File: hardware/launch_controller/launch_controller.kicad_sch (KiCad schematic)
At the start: 32 parts, among them IC1 ADIN1110BCPZ, J1 Screw_Terminal_01x03, T1 Transformer_1P_1S, Y1 25MHz

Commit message: feat(scm): STM32 added.
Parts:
- added C17, C9: 1μF, Package_TO_SOT_SMD:TSOT-23-6, symbol Device:C_Small
- added C18, C19: 22μF, symbol Device:C_Small
- added D2: LED, Package_DFN_QFN:Texas_RPU0010A_VQFN-HR-10_2x2mm_P0.5mm, symbol Device:LED
- added J2: Conn_01x02_Socket, Converter_DCDC:Converter_DCDC_Murata_MYRxP, symbol Connector:Conn_01x02_Socket
- added L1: 4.7μH, Package_SO:SOIC-16_3.9x9.9mm_P1.27mm, symbol Device:L_Small
- added R7: 1kΩ, symbol Device:R
- added R8: 4.7kΩ, symbol Device:R
- added U1: STM32U575VITx, Package_QFP:LQFP-100_14x14mm_P0.5mm, symbol MCU_ST_STM32U5:STM32U575VITx
- added U2: AP63205WU, Package_TO_SOT_SMD:TSOT-23-6, symbol Regulator_Switching:AP63205WU
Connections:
- net +3.3V: now also R4.1, C18.1, C19.2, L1.2, R7.1, R8.1, U1.100 (VDD), U1.11 (VDD), U1.21 (VREF+), U1.22 (VDDA), U1.28 (VDD), U1.50 (VDD), U1.75 (VDD), U2.1 (FB)
- net EC_INT: now also U1.67 (PA8)
- net EC_RESET: now also U1.23 (PA0)
- net EC_SPI_CS: now also U1.29 (PA4)
- net EC_SPI_MISO: now also U1.31 (PA6)
- net EC_SPI_MOSI: now also U1.32 (PA7)
- net EC_SPI_SCLK: now also U1.30 (PA5)
- net GND: now also C18.2, C19.1, C9.2, J2.2 (Pin_2), U1.10 (VSS), U1.19 (VSSA), U1.27 (VSS), U1.49 (VSS), U1.74 (VSS), U1.99 (VSS), U2.4 (GND); no longer R4.1
- net EC_STATUS: now reaches IC1.3 (LED_0)
- net EC_STATUS: now also D2.1 (K), R8.2
- new net: C9.1, J2.1 (Pin_1), U2.2 (EN), U2.3 (IN)
- new net: C17.1, L1.1, U2.5 (SW)
- new net: C17.2, U2.6 (BST)
- new net: D2.2 (A), R7.2
- new net UART_STM32_RX: U1.69 (PA10)
- new net UART_STM32_TX: U1.68 (PA9)
- no-connect marks 15 -> 14
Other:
- note added: "Conntroller"
- note removed: "Controller"

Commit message: feat(scm): USB added.
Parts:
- removed U2: AP63205WU, Package_TO_SOT_SMD:TSOT-23-6, symbol Regulator_Switching:AP63205WU
- added C20: 0.1μF, symbol Device:C_Small
- added D3: LED, Package_DFN_QFN:Texas_RPU0010A_VQFN-HR-10_2x2mm_P0.5mm, symbol Device:LED
- added J3: USB_B, symbol Connector:USB_B
- added R10, R9: R, symbol Device:R
- added R11: 4.7μF, symbol Device:R
- added R18: 1kΩ, symbol Device:R
- added R19: 10kΩ, symbol Device:R
- added R20: 22kΩ, symbol Device:R
- added U2: AP63203WU, Package_TO_SOT_SMD:TSOT-23-6, symbol Regulator_Switching:AP63203WU
- added U3: SN74LVC257AD, D16, symbol pCloud:SN74LVC257AD
- added U4: FT232H, symbol Interface_USB:FT232H
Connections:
- net +3.3V: now also U1.6 (VBAT), U1.73 (VDDUSB), R18.1, U2.1 (FB), U3.16 (VCC)
- net EC_SPI_CS: now also U3.4 (1Y); no longer U1.29 (PA4)
- net EC_SPI_MISO: now also U3.9 (3Y); no longer U1.31 (PA6)
- net EC_SPI_MOSI: now also U3.12 (4Y); no longer U1.32 (PA7)
- net EC_SPI_SCLK: now also U3.7 (2Y); no longer U1.30 (PA5)
- net GND: now also U1.20 (VREF-), C20.1, D3.1 (K), R10.2, R11.1, R20.1, U2.4 (GND), U3.15 (*OE), U3.8 (GND)
- net at C9.1, J2.1 (Pin_1): now also R9.1, U2.2 (EN), U2.3 (IN)
- net at C17.1, L1.1: now also U2.5 (SW)
- net at C17.2: now also U2.6 (BST)
- net at U1.14 (NRST): now also C20.2
- net ADC: now reaches U1.24 (PA1)
- net ADC: now also R10.1, R9.2
- net at U1.48 (VCAP): now also R11.2
- new net: R19.2, R20.2, U3.1 (*A/B)
- new net: D3.2 (A), R18.2
- new net MCU_SPI_CS: U1.29 (PA4), U3.2 (1A)
- new net MCU_SPI_MISO: U1.31 (PA6), U3.11 (3A)
- new net MCU_SPI_MOSI: U1.32 (PA7), U3.14 (4A)
- new net MCU_SPI_SCLK: U1.30 (PA5), U3.5 (2A)
- new net VBUS: J3.1 (VBUS), R19.1
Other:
- note added: "MCU"
- note added: "Power"
- moved on the sheet: C17, C18, C19, C9, D2, J2, L1, R7, R8, U1

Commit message: feat(scm): Draft v1.
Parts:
- removed U3: SN74LVC257AD, D16, symbol pCloud:SN74LVC257AD
- removed U4: FT232H, symbol Interface_USB:FT232H
- added C21, C22, C27: 0.1μF, symbol Device:C_Small
- added C23: 4.7μF, symbol Device:C_Small
- added C24: 10nF, symbol Device:C_Small
- added C25, C26: 47pF, symbol Device:C_Small
- added D4, D5: D_Small, symbol Device:D_Small
- added D6, D7, D8, D9: LED, symbol Device:LED
- added FB1: FerriteBead, symbol Device:FerriteBead
- added R21, R22, R23, R24, R25, R26, R27, R28: 10kΩ, symbol Device:R
- added SW1, SW2, SW3, SW4, SW5: SW_SPST, symbol Switch:SW_SPST
- added U3: FT230XS, Package_SO:SSOP-16_3.9x4.9mm_P0.635mm, symbol Interface_USB:FT230XS
- C9: value 1μF -> 10μF
- R19: value 10kΩ -> 27Ω
- R20: value 22kΩ -> 27Ω
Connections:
- net MCU_SPI_CS is gone; now on net EC_SPI_CS: U1.29 (PA4)
- net MCU_SPI_MISO is gone; now on net EC_SPI_MISO: U1.31 (PA6)
- net MCU_SPI_MOSI is gone; now on net EC_SPI_MOSI: U1.32 (PA7)
- net MCU_SPI_SCLK is gone; now on net EC_SPI_SCLK: U1.30 (PA5)
- net +3.3V: now also R21.1, R22.1, R23.1, R24.1, R25.1, R26.1, R27.1, R28.1
- net ADC: now also C27.2
- net GND: now also J3.4 (GND), J3.SH (Shield), C21.1, C22.1, C23.1, C24.1, C25.2, C26.1, C27.1, D6.1 (K), D6.2 (A), D7.1 (K), D7.2 (A), D8.1 (K), D8.2 (A), D9.1 (K), D9.2 (A), R22.2, R24.2, R26.2, R28.2, SW1.2 (B), SW2.2 (B), SW3.2 (B), SW4.2 (B), U3.13 (GND), U3.5 (GND); no longer R20.1
- net UART_STM32_RX: now also U3.1 (TXD)
- net UART_STM32_TX: now also U3.4 (RXD)
- net VBUS: now also C24.2, D5.2 (A), FB1.1; no longer R19.1
- net at C9.1, R9.1, U2.2 (EN)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: now also D4.1 (K), D5.1 (K); no longer J2.1 (Pin_1)
- net at R20.2: now also U3.9 (USBDM); no longer R19.2
- net at J3.2 (D-): now also R20.1, C26.2
- net at J3.3 (D+): now also R19.1, C25.1
- new net: D4.2 (A), SW5.2 (B)
- new net: C22.2, C23.2, FB1.2, U3.12 (VCC)
- new net: C21.2, U3.10 (3V3OUT), U3.11 (~{RESET}), U3.3 (VCCIO)
- new net: R19.2, U3.8 (USBDP)
- new net +12V: J2.1 (Pin_1), SW5.1 (A)
- new net GPIO_DUMP: R23.2, SW2.1 (A)
- new net GPIO_FILL: R21.2, R27.2, SW1.1 (A), SW4.1 (A)
- new net GPIO_GOX: R25.2, SW3.1 (A)
- no-connect marks 14 -> 93
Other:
- note added: "Hybrid Circit"
- note added: "Status"
- note added: "Switches"
- note added: "USB"
- note removed: "Connector"
- moved on the sheet: C17, C18, C19, C20, C9, D2, D3, J2, L1, R10, R11, R18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

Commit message: fix(scm): Hybrid circit updated.
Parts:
- added C28, C29: 47pF, symbol Device:C_Small
- added D10: D_TVS_Dual_AAC, Package_TO_SOT_SMD:TSOT-23-5_HandSoldering, symbol Device:D_TVS_Dual_AAC
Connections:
- net EC_RXN: now also R13.1, R15.1; no longer R12.2, R16.1
- net EC_RXP: now also R12.2, R17.1; no longer R12.1, R15.1
- net EC_TXN: now also R12.1, R14.1; no longer R13.2, R17.1
- net EC_TXP: now also R13.2, R16.1; no longer R13.1, R14.1
- net GND: now also C28.2, C29.2, D10.3 (common)
- net at C15.1, R16.2, R17.2: now also D1.2 (A2)
- net at C14.1, R14.2, R15.2: now also D1.1 (A1)
- net at J1.1 (Pin_1), T1.4 (SB): now also C28.1, D10.2 (A2)
- net SPE_1: no longer names the net of C14.2, T1.1 (AA)
- net SPE_1: no longer D1.1 (A1)
- net SPE_2: no longer names the net of C15.2, T1.2 (AB)
- net SPE_2: no longer D1.2 (A2)
- new net: C29.1, D10.1 (A1)
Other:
- moved on the sheet: C14, C15, C16, D1, J1, R12, R13, R14, R15, T1

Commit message: feat(scm): USB Surge Protection Circuit
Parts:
- added C30, C31, C32, C33, C34, C35, C36, C37: 0.1nF, symbol Device:C_Small
- added C38: 1μF, symbol Device:C_Small
- added C39: 10μF, symbol Device:C_Small
- added C40: 4.7nF, symbol Device:C_Small
- added R11: 1MΩ, symbol Device:R
- added SW6: SW_SPST, symbol Switch:SW_SPST
- added U5: USBLC6-2P6, Package_TO_SOT_SMD:SOT-666, symbol Power_Protection:USBLC6-2P6
- C1: value 0.01μF -> 0.1μF
- C11: renamed from R11; symbol Device:R -> Device:C_Small
- C17: value 1μF -> 0.1μF
- L1: value 4.7μH -> 3.9μH
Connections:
- net +3.3V: now also C1.2, C10.2, C11.2, C12.1, C13.1, C16.2, C18.2, C19.1, C2.2, C20.1, C21.1, C22.1, C23.1, C24.1, C25.2, C26.1, C27.1, C28.2, C29.2, C3.1, C4.1, C5.1, C6.1, C7.2, C8.2, C9.2, D1.3 (common), D10.3 (common), D3.1 (K), D6.1 (K), D6.2 (A), D7.1 (K), D7.2 (A), D8.1 (K), D8.2 (A), D9.1 (K), D9.2 (A), IC1.41 (GND), J2.2 (Pin_2), J3.4 (GND), R10.2, R22.2, R24.2, R26.2, R28.2, R3.1, R5.2, SW1.2 (B), SW2.2 (B), SW3.2 (B), SW4.2 (B), U1.10 (VSS), U1.19 (VSSA), U1.20 (VREF-), U1.27 (VSS), U1.49 (VSS), U1.74 (VSS), U1.99 (VSS), U2.4 (GND), U3.13 (GND), U3.5 (GND), C30.1, C31.1, C32.1, C33.1, C34.1, C35.1, C36.1, C37.1, C38.1, C39.1, C40.1, R11.2, U5.2 (GND)
- net VBUS: now also U5.5 (VBUS)
- net at D1.2 (A2), R16.2, R17.2: now also T1.2 (AB); no longer C15.1
- net at C25.1, R19.1: now also U5.6 (I/O1); no longer J3.3 (D+)
- net at D1.1 (A1), R14.2, R15.2: now also T1.1 (AA); no longer C14.1
- net at C14.2: now also C28.1, D10.2 (A2), J1.1 (Pin_1); no longer T1.1 (AA)
- net at C11.2: no longer U1.48 (VCAP)
- net at C26.2, R20.1: now also U5.4 (I/O2); no longer J3.2 (D-)
- net at C15.2: now also J1.2 (Pin_2); no longer T1.2 (AB)
- net at T1.3 (SA): now also C15.1; no longer J1.2 (Pin_2)
- net at C20.2: now also SW6.1 (A); no longer U1.14 (NRST)
- removed net GND: C1.2, C10.2, C11.1, C11.2, C12.1, C13.1, C16.2, C18.2, C19.1, C2.2, C20.1, C21.1, C22.1, C23.1, C24.1, C25.2, C26.1, C27.1, C28.2, C29.2, C3.1, C4.1, C5.1, C6.1, C7.2, C8.2, C9.2, D1.3 (common), D10.3 (common), D3.1 (K), D6.1 (K), D6.2 (A), D7.1 (K), D7.2 (A), D8.1 (K), D8.2 (A), D9.1 (K), D9.2 (A), IC1.41 (GND), J2.2 (Pin_2), J3.4 (GND), J3.SH (Shield), R10.2, R22.2, R24.2, R26.2, R28.2, R3.1, R5.2, SW1.2 (B), SW2.2 (B), SW3.2 (B), SW4.2 (B), U1.10 (VSS), U1.19 (VSSA), U1.20 (VREF-), U1.27 (VSS), U1.49 (VSS), U1.74 (VSS), U1.99 (VSS), U2.4 (GND), U3.13 (GND), U3.5 (GND)
- new net: C30.2, C31.2, C32.2, C33.2, C34.2, C35.2, C36.2, C37.2, C38.2, C39.2
- new net: C14.1, T1.4 (SB)
- new net: J3.2 (D-), U5.3 (I/O2)
- new net: J3.3 (D+), U5.1 (I/O1)
- new net: SW6.2 (B), U1.14 (NRST)
- new net Earth: C40.2, J3.SH (Shield), R11.1
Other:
- moved on the sheet: C20, C25, C26, FB1, R19, R20, T1

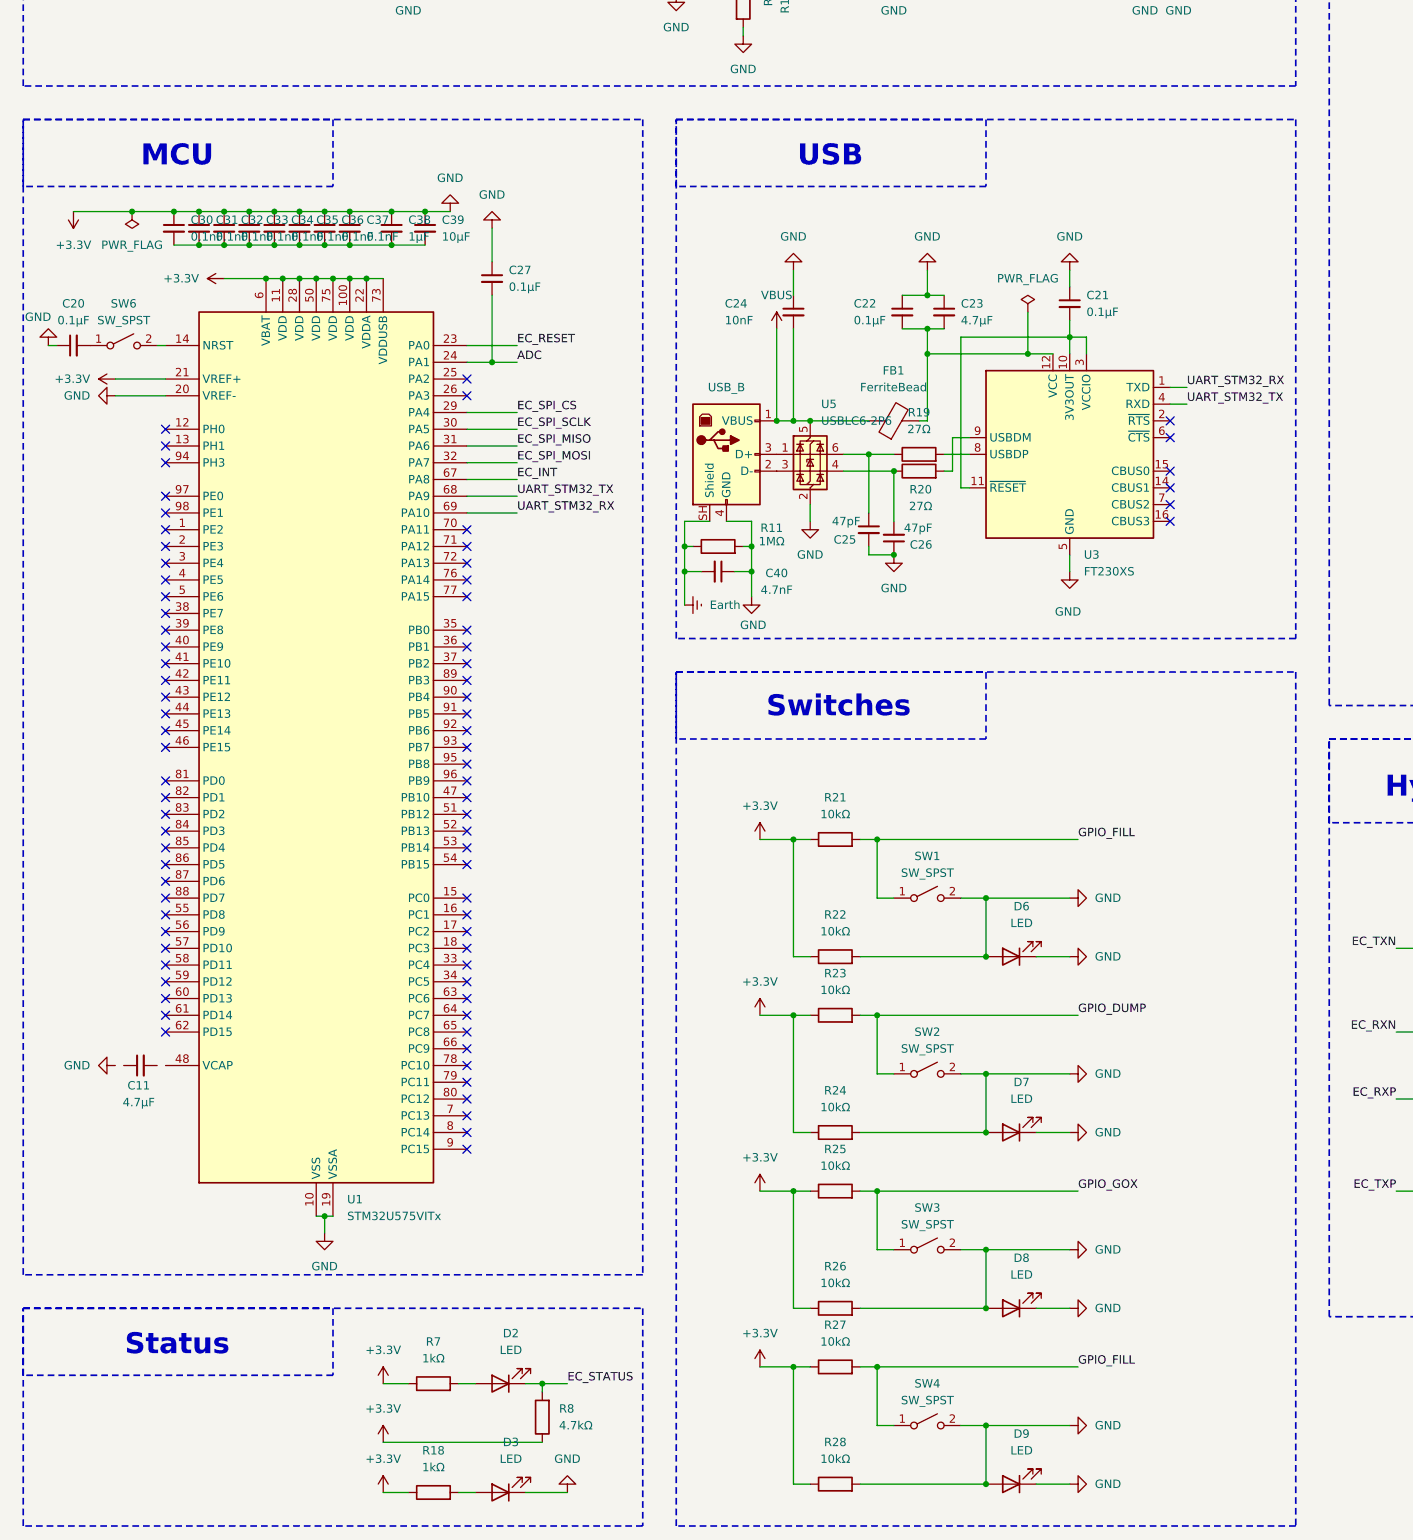
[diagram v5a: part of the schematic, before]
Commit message: fix(scm): TBD62083A amd SWD are added.
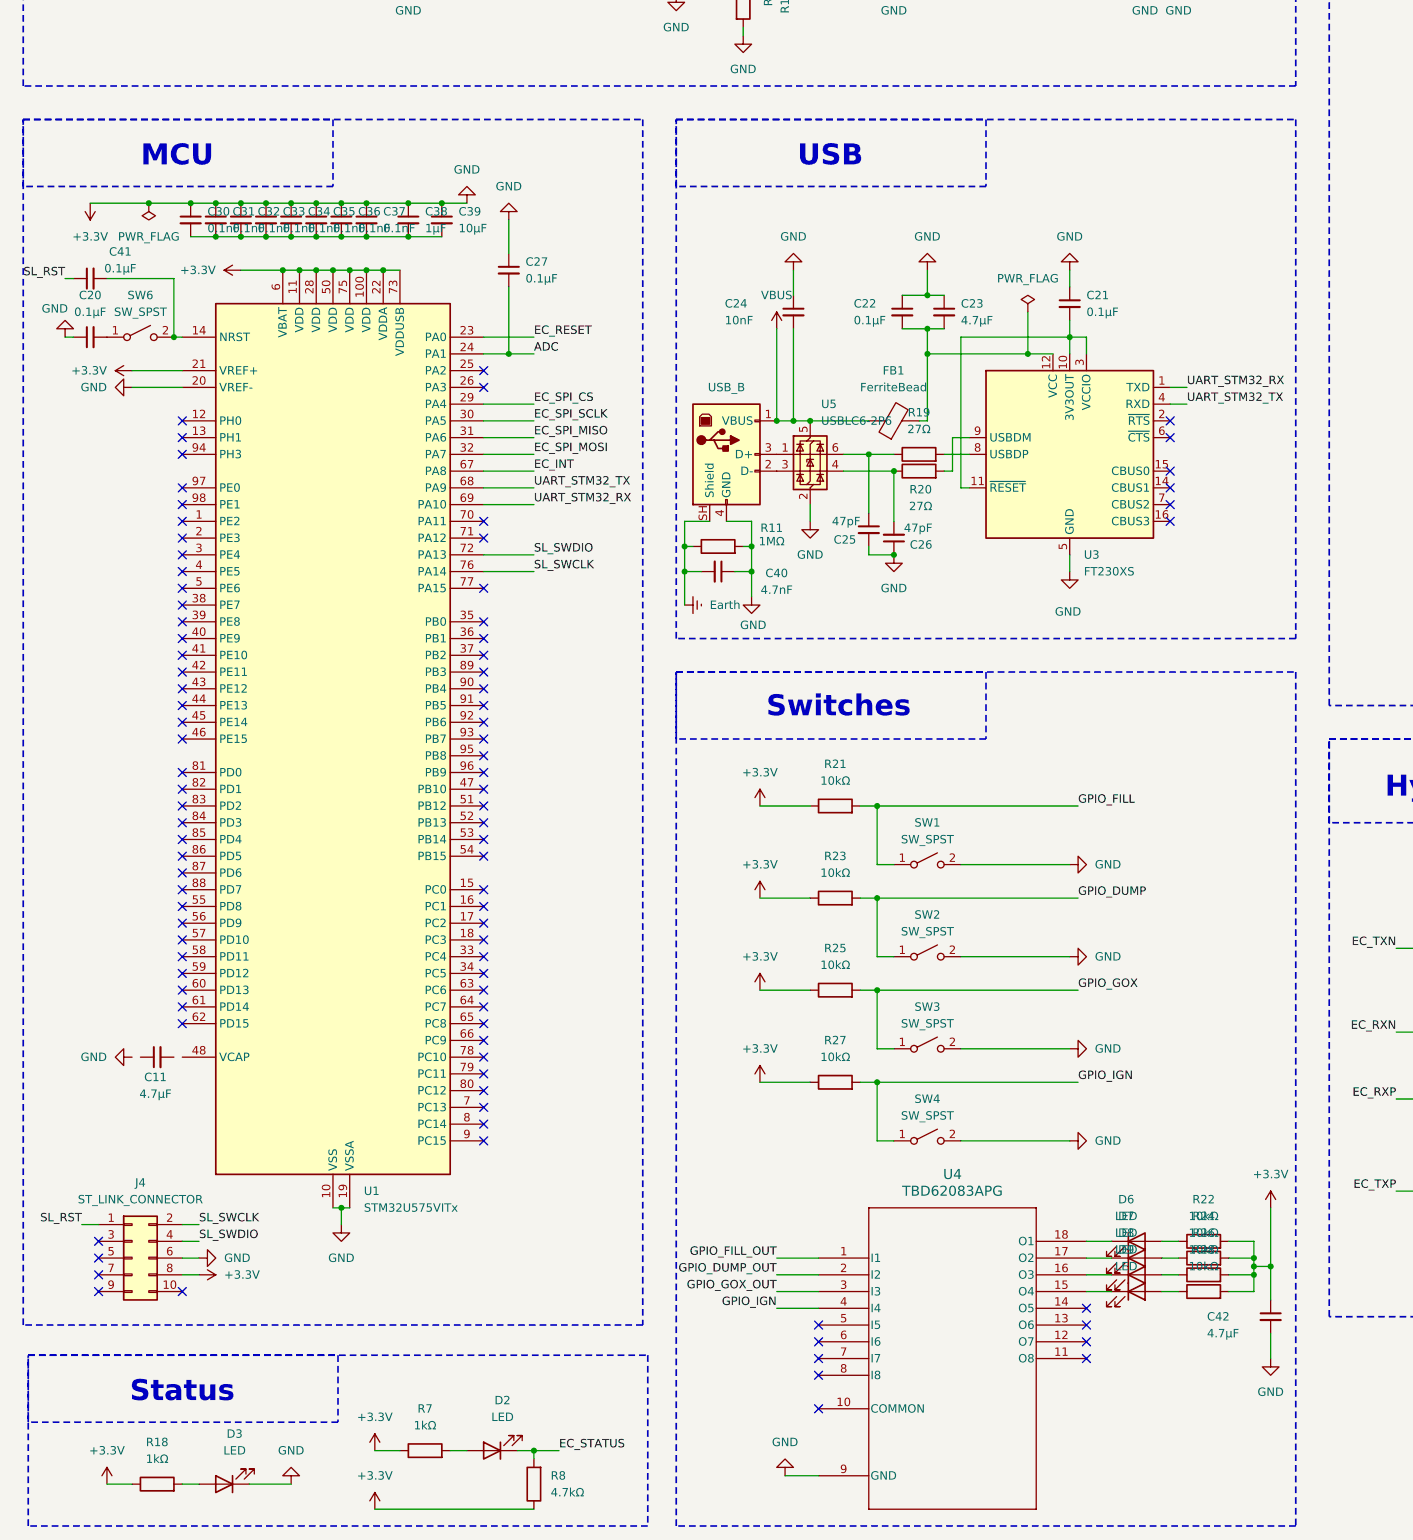
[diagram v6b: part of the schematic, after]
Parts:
- added C41: 0.1μF, symbol Device:C_Small
- added C42: 4.7μF, symbol Device:C_Small
- added J4: ST_LINK_CONNECTOR, symbol Connector_Generic:Conn_02x05_Odd_Even
- added U4: TBD62083APG, P-DIP18-300-2p54-001_TOS, symbol pCloud:TBD62083APG
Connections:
- net +3.3V: now also C42.1, C42.2, J4.6 (Pin_6), J4.8 (Pin_8), U4.9 (GND); no longer D6.1 (K), D6.2 (A), D7.1 (K), D7.2 (A), D8.1 (K), D8.2 (A), D9.1 (K), D9.2 (A), R22.1, R24.1, R26.1, R28.1
- net GPIO_FILL: no longer R27.2, SW4.1 (A)
- net at SW6.2 (B), U1.14 (NRST): now also C41.2
- net SL_SWDIO: now reaches U1.72 (PA13)
- net SL_SWDIO: now also J4.4 (Pin_4)
- net SL_SWCLK: now reaches U1.76 (PA14)
- net SL_SWCLK: now also J4.2 (Pin_2)
- new net: D6.1 (K), U4.18 (O1)
- new net: D6.2 (A), R22.1
- new net: D7.2 (A), R24.1
- new net: D9.2 (A), R28.1
- new net: D8.2 (A), R26.1
- new net: D9.1 (K), U4.15 (O4)
- new net: D8.1 (K), U4.16 (O3)
- new net: D7.1 (K), U4.17 (O2)
- new net GPIO_DUMP_OUT: U4.2 (I2)
- new net GPIO_FILL_OUT: U4.1 (I1)
- new net GPIO_GOX_OUT: U4.3 (I3)
- new net GPIO_IGN: R27.2, SW4.1 (A), U4.4 (I4)
- new net SL_RST: C41.1, J4.1 (Pin_1)
- no-connect marks 93 -> 105
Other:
- moved on the sheet: C11, C20, C27, C30, C31, C32, C33, C34, C35, C36, C37, C38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
